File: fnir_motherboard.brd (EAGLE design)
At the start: 33.6 x 43.5 mm, 44 parts, among them IC1 LTC2494, IC3 AD712R, U2 ATMEGA8U2QFN, X2 USB-SMD-NS, Y1 16MHz

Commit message: new version desinged
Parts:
- added R16: 200, adafruit:R1206
- added TP1: PTR1B1,27, testpad:B1,27
- C1, C2, C3, C4, C5, C6, C7, C8: device adafruit:C0805 -> adafruit:C1206
- C10, C9: value (none) -> 0.1uF; device adafruit:C0805 -> adafruit:C1206
- R1: value (none) -> 200; device adafruit:R0805 -> adafruit:R1206
- R10, R11, R12, R13, R14, R15, R28, R29, R5, R6, R7, R8, R9: device adafruit:R0805 -> adafruit:R1206
- R2: value (none) -> 10k
- R3, R4: value (none) -> 30k; device adafruit:R0805 -> adafruit:R1206
- U2: value ATMEGA8U2QFN -> ATMEGA8U2AU; device sparkfun:QFN-32 -> sparkfun:TQFP32-08
- moved X2 34.2 mm to (11.7, 4.76), turned to 90 degrees
- moved R3 30.0 mm to (47.0, 25.4)
- moved C9 30.0 mm to (44.8, 25.4)
- moved C10 28.5 mm to (46.0, 21.6), turned to 0 degrees
- moved Q6 27.1 mm to (42.5, 15.2), turned to 180 degrees
- moved R14 24.2 mm to (42.5, 3.81), turned to 90 degrees
- moved R15 21.9 mm to (8.41, 33.3)
- moved LED1 21.9 mm to (19.5, 33.5)
- moved R1 21.9 mm to (19.5, 31.3)
- moved R29 21.0 mm to (13.3, 12.4), turned to 90 degrees
- moved Q4 20.8 mm to (37.5, 15.2), turned to 180 degrees
- moved Q7 20.8 mm to (40.0, 17.8), turned to 180 degrees
- moved R13 20.7 mm to (40.0, 3.81), turned to 90 degrees
- moved R4 19.1 mm to (46.0, 29.2), turned to 180 degrees
- moved U2 18.7 mm to (11.4, 26.7), turned to 90 degrees
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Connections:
- new net N$23: R16.2, SV1.2
- net +5V: now also R2.1; no longer R2.3
- net AGND: now also R2.3; no longer R2.1
- net GND: now also R16.1; no longer SV1.2
- net IR8: now also IC1.17; no longer IC1.16
- net IR9: now also IC1.19; no longer IC1.17
- net N$1: now also Q2.1; no longer Q6.1
- net N$12: now also TP1.TP
- net N$2: now also Q1.1; no longer Q7.1
- net N$3: now also Q9.1, U2.11; no longer Q5.1, U2.10
- net N$4: now also Q4.1; no longer Q1.1
- net N$5: now also Q5.1; no longer Q4.1
- net N$6: now also Q7.1; no longer Q9.1
- net N$7: now also Q6.1; no longer Q2.1
- net N$8: now also U2.10; no longer U2.11
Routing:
- net +5V: track 212.0 -> 116.5 mm, vias 8 -> 3
- net IR8: track 34.0 -> 63.7 mm
- net IR9: track 37.6 -> 67.3 mm
- net IR7: track 30.4 -> 58.8 mm
- net N$7: track 13.3 -> 41.7 mm
- net IR6: track 26.7 -> 53.8 mm
- net IR5: track 22.9 -> 49.1 mm
- net IR4: track 19.2 -> 44.9 mm
- net N$6: track 17.1 -> 42.7 mm
- net IR3: track 16.3 -> 41.3 mm
- net IR2: track 13.6 -> 37.5 mm
- net IR1: track 10.8 -> 34.1 mm
- net IR0: track 7.57 -> 29.8 mm
- net N$4: track 19.8 -> 40.1 mm
- net N$3: track 7.57 -> 27.4 mm, vias 0 -> 2
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- added copper zone on layer 1, net +5V
- removed copper zone on layer 16, net AGND
- removed copper zone on layer 16, net GND
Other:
- board size 33.6 x 43.5 mm -> 50 x 35.7 mm
- board text added: "ADC Neg Ref"
- board text added: "Jeremy Ruhland"
- board text added: "fNIR Neural Imaging Mobo"
- board text added: "github.com/JeremyRuhland/fnir"

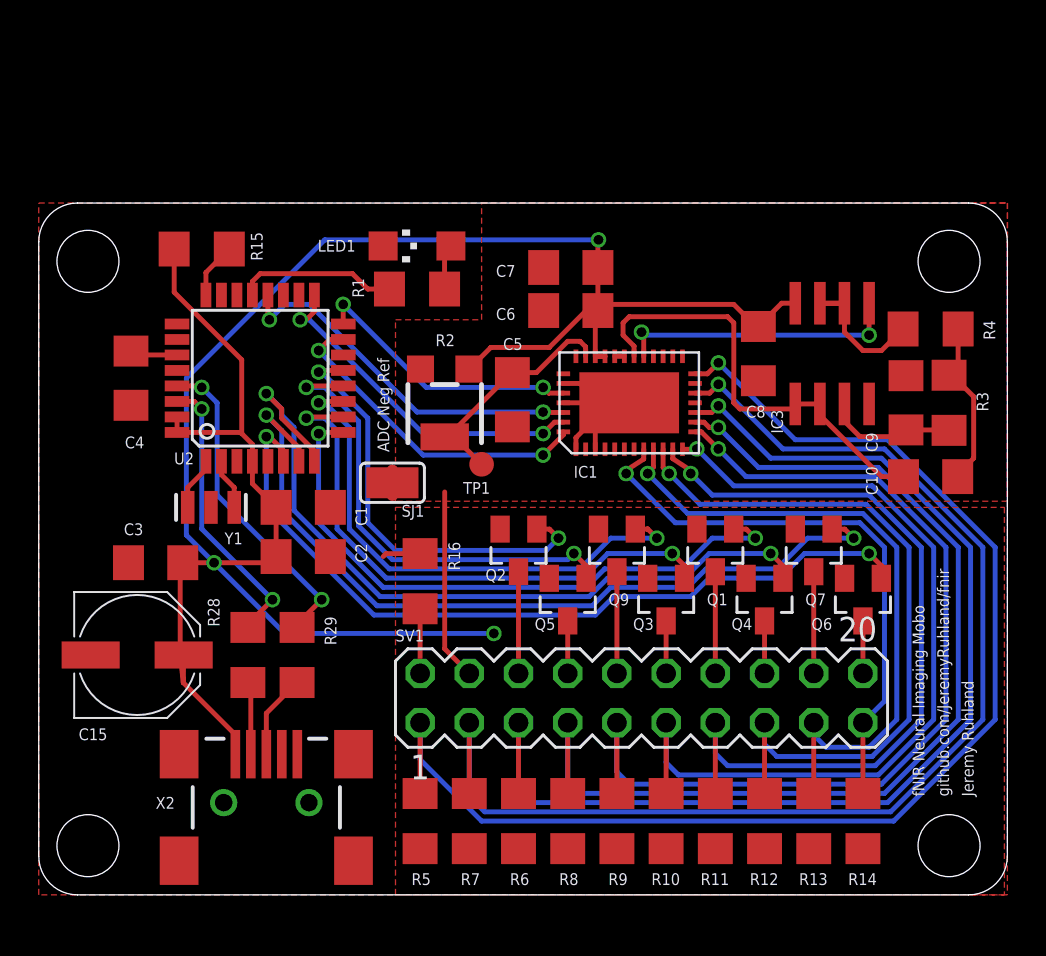
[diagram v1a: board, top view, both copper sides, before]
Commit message: slight changes to pour layouts for ground and agnd (merged)
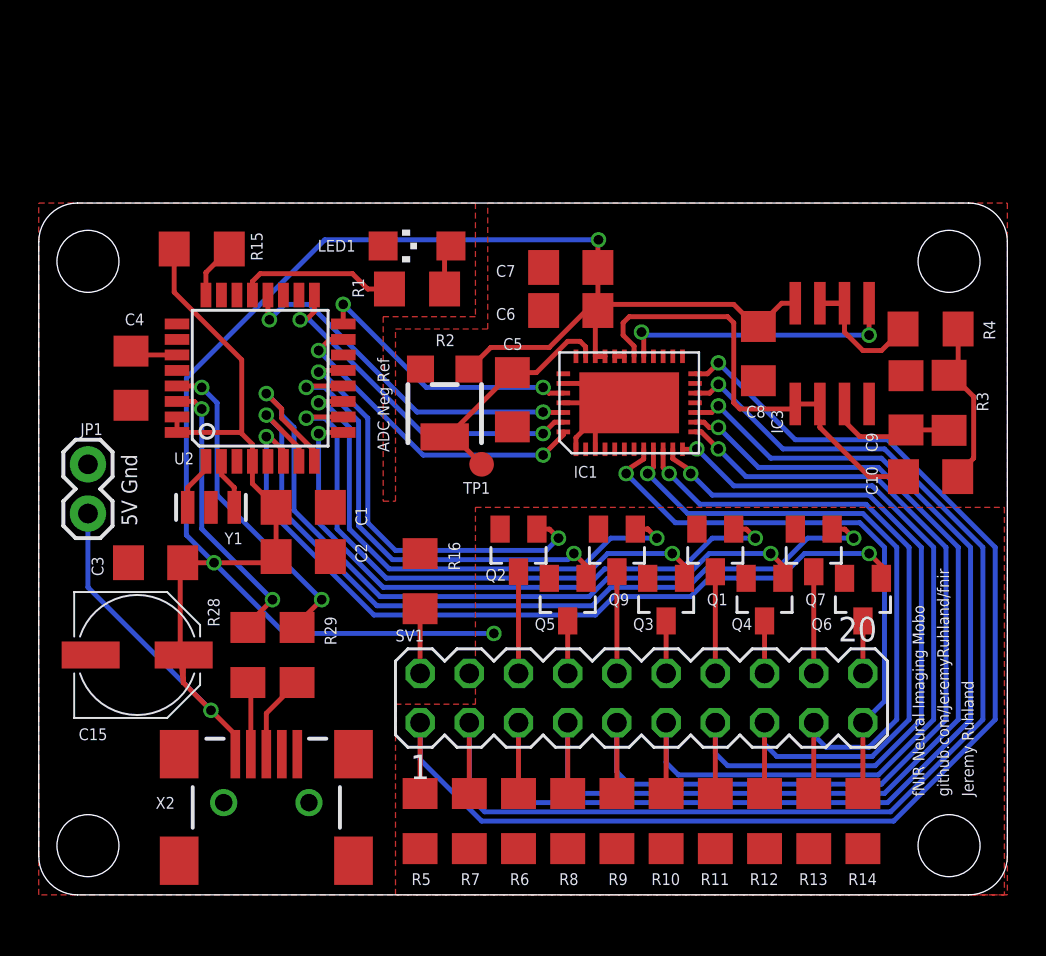
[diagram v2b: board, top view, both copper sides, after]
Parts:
- removed SJ1: (no value), jumper:SJ
- added JP1: (no value), sparkfun:1X02
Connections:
- removed net AGND: C5.2, C6.2, C7.2, C8.2, C9.2, IC1.1, IC1.3, IC1.31, IC1.32, IC1.33, IC1.35, IC1.4, IC1.5, IC1.6, IC1.7, IC1.P, IC3.4, R2.3, SJ1.1, SV1.4
- net +5V: now also JP1.2
- net GND: now also C5.2, C6.2, C7.2, C8.2, C9.2, IC1.1, IC1.3, IC1.31, IC1.32, IC1.33, IC1.35, IC1.4, IC1.5, IC1.6, IC1.7, IC1.P, IC3.4, JP1.1, R2.3, SV1.4; no longer SJ1.2
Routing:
- net AGND: track 18.0 -> 0.00 mm
- net +5V: track 116.5 -> 129.3 mm, vias 3 -> 4
- net GND: track 1.97 -> 8.12 mm
- net N$22: track 1.27 -> 0.00 mm
- removed copper zone on layer 1, net AGND
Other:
- board text added: "5V Gnd"

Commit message: updated sch and makefile for 16u2, more space to fit firmware with dfu usb bootloader
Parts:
- U2: value ATMEGA8U2AU -> ATMEGA16U2AU
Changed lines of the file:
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@@
 <attribute name="VALUE" x="3.33" y="10.4075" size="0.6096" layer="27"/>
 </element>
-<element name="U2" library="sparkfun" package="TQFP32-08" value="ATMEGA8U2AU" x="11.43" y="26.67" smashed="yes" rot="R90">
+<element name="U2" library="sparkfun" package="TQFP32-08" value="ATMEGA16U2AU" x="11.43" y="26.67" smashed="yes" rot="R90">
 <attribute name="NAME" x="6.985" y="22.225" size="0.6096" layer="25"/>
 <attribute name="VALUE" x="17.78" y="24.13" size="0.6096" layer="27" rot="R90"/>
